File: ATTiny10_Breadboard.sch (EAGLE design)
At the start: 5 parts, among them IC1 ATTINY4/5/9/10, J1 ISP/TPI-6PIN

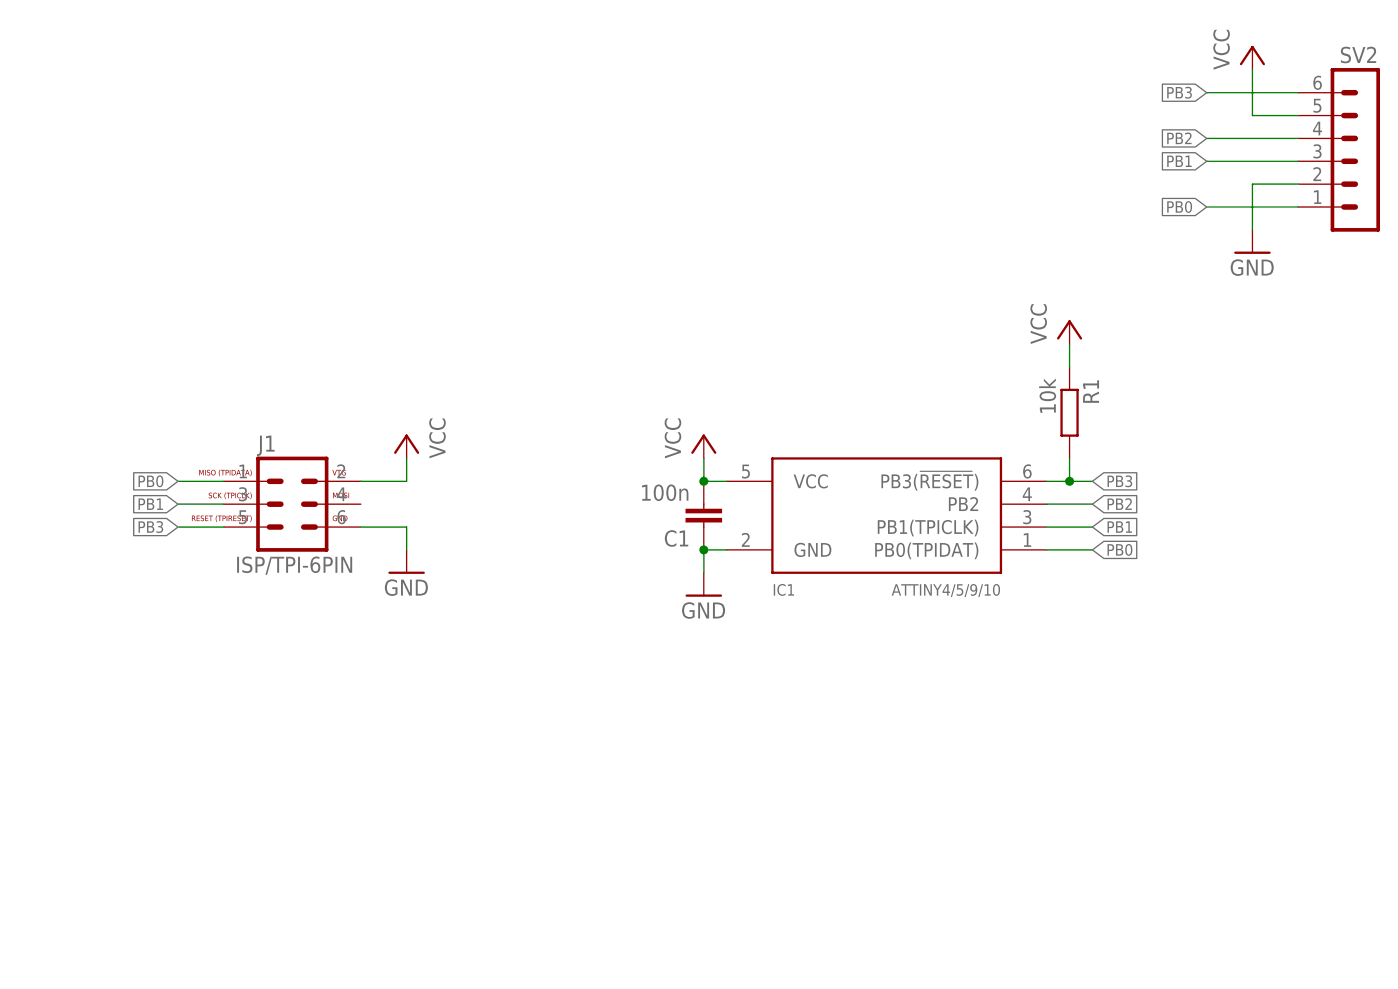
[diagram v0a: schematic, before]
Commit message: Fixed Tiny10 Board: Now there's an option to connect MISO and MOSI for USBasp compatibility
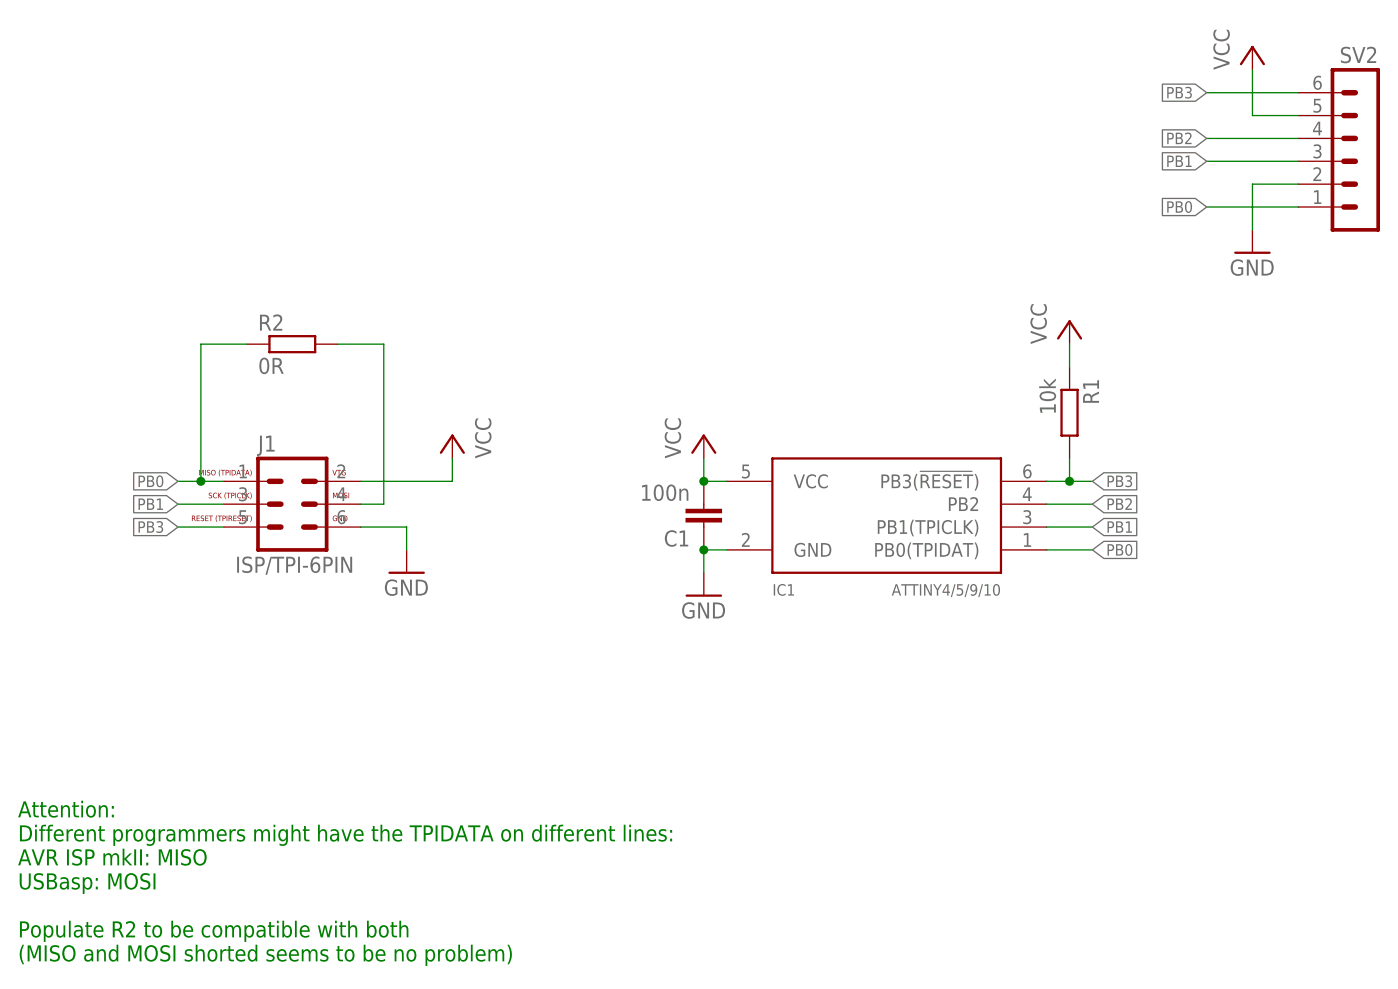
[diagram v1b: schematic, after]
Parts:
- added R2: 0R, rcl:R-EU_R0402
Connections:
- new net N$1: J1.4, R2.2
- net PB0: now also R2.1
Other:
- note added: "Attention: Different programmers might have the TPIDATA on different lines: AVR ISP mkII: MISO USBasp: MOSI Populate R2 to be compatible with both (MISO and MOSI shorted seems to be no problem)"
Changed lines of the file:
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@@
 <part name="R1" library="rcl" library_urn="urn:adsk.eagle:library:334" deviceset="R-EU_" device="R0402" package3d_urn="urn:adsk.eagle:package:23547/3" value="10k"/>
 <part name="P+4" library="supply1" library_urn="urn:adsk.eagle:library:371" deviceset="VCC" device=""/>
+<part name="R2" library="rcl" library_urn="urn:adsk.eagle:library:334" deviceset="R-EU_" device="R0402" package3d_urn="urn:adsk.eagle:package:23547/3" value="0R"/>
 </parts>
 <sheets>
 <sheet>
 <plain>
+<text x="7.62" y="7.62" size="1.778" layer="91">Attention:
+Different programmers might have the TPIDATA on different lines:
+AVR ISP mkII: MISO
+USBasp: MOSI
+Populate R2 to be compatible with both
+(MISO and MOSI shorted seems to be no problem)</text>
 </plain>
 <instances>
@@
 <attribute name="VALUE" x="81.28" y="63.5" size="1.778" layer="96" rot="R90"/>
 </instance>
-<instance part="P+2" gate="VCC" x="50.8" y="66.04" smashed="yes" rot="MR0">
-<attribute name="VALUE" x="53.34" y="63.5" size="1.778" layer="96" rot="MR90"/>
+<instance part="P+2" gate="VCC" x="55.88" y="66.04" smashed="yes" rot="MR0">
+<attribute name="VALUE" x="58.42" y="63.5" size="1.778" layer="96" rot="MR90"/>
 </instance>
 <instance part="P+3" gate="VCC" x="144.78" y="109.22" smashed="yes">
@@
 <instance part="P+4" gate="VCC" x="124.46" y="78.74" smashed="yes">
 <attribute name="VALUE" x="121.92" y="76.2" size="1.778" layer="96" rot="R90"/>
+</instance>
+<instance part="R2" gate="G$1" x="38.1" y="76.2" smashed="yes">
+<attribute name="NAME" x="34.29" y="77.6986" size="1.778" layer="95"/>
+<attribute name="VALUE" x="34.29" y="72.898" size="1.778" layer="96"/>
 </instance>
 </instances>
@@
 <pinref part="J1" gate="G$1" pin="2"/>
 <pinref part="P+2" gate="VCC" pin="VCC"/>
-<wire x1="45.72" y1="60.96" x2="50.8" y2="60.96" width="0.1524" layer="91"/>
-<wire x1="50.8" y1="60.96" x2="50.8" y2="63.5" width="0.1524" layer="91"/>
+<wire x1="45.72" y1="60.96" x2="55.88" y2="60.96" width="0.1524" layer="91"/>
+<wire x1="55.88" y1="60.96" x2="55.88" y2="63.5" width="0.1524" layer="91"/>
 </segment>
 <segment>
@@
 <segment>
 <pinref part="J1" gate="G$1" pin="1"/>
-<wire x1="25.4" y1="60.96" x2="30.48" y2="60.96" width="0.1524" layer="91"/>
+<wire x1="25.4" y1="60.96" x2="27.94" y2="60.96" width="0.1524" layer="91"/>
 <label x="25.4" y="60.96" size="1.27" layer="95" rot="R180" xref="yes"/>
+<pinref part="R2" gate="G$1" pin="1"/>
+<wire x1="27.94" y1="60.96" x2="30.48" y2="60.96" width="0.1524" layer="91"/>
+<wire x1="33.02" y1="76.2" x2="27.94" y2="76.2" width="0.1524" layer="91"/>
+<wire x1="27.94" y1="76.2" x2="27.94" y2="60.96" width="0.1524" layer="91"/>
+<junction x="27.94" y="60.96"/>
+</segment>
+</net>
+<net name="N$1" class="0">
+<segment>
+<pinref part="J1" gate="G$1" pin="4"/>
+<wire x1="45.72" y1="58.42" x2="48.26" y2="58.42" width="0.1524" layer="91"/>
+<wire x1="48.26" y1="58.42" x2="48.26" y2="76.2" width="0.1524" layer="91"/>
+<pinref part="R2" gate="G$1" pin="2"/>
+<wire x1="48.26" y1="76.2" x2="43.18" y2="76.2" width="0.1524" layer="91"/>
 </segment>
 </net>
@@
 </drawing>
 <compatibility>
+<note version="6.3" minversion="6.2.2" severity="warning">
+Since Version 6.2.2 text objects can contain more than one line,
+which will not be processed correctly with this version.
+</note>
 <note version="8.2" severity="warning">
 Since Version 8.2, EAGLE supports online libraries. The ids
